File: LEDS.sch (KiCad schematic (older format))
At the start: 76 parts, among them Q1 MOSFET_N, Q2 MOSFET_N, Q3 MOSFET_N, Q4 MOSFET_N

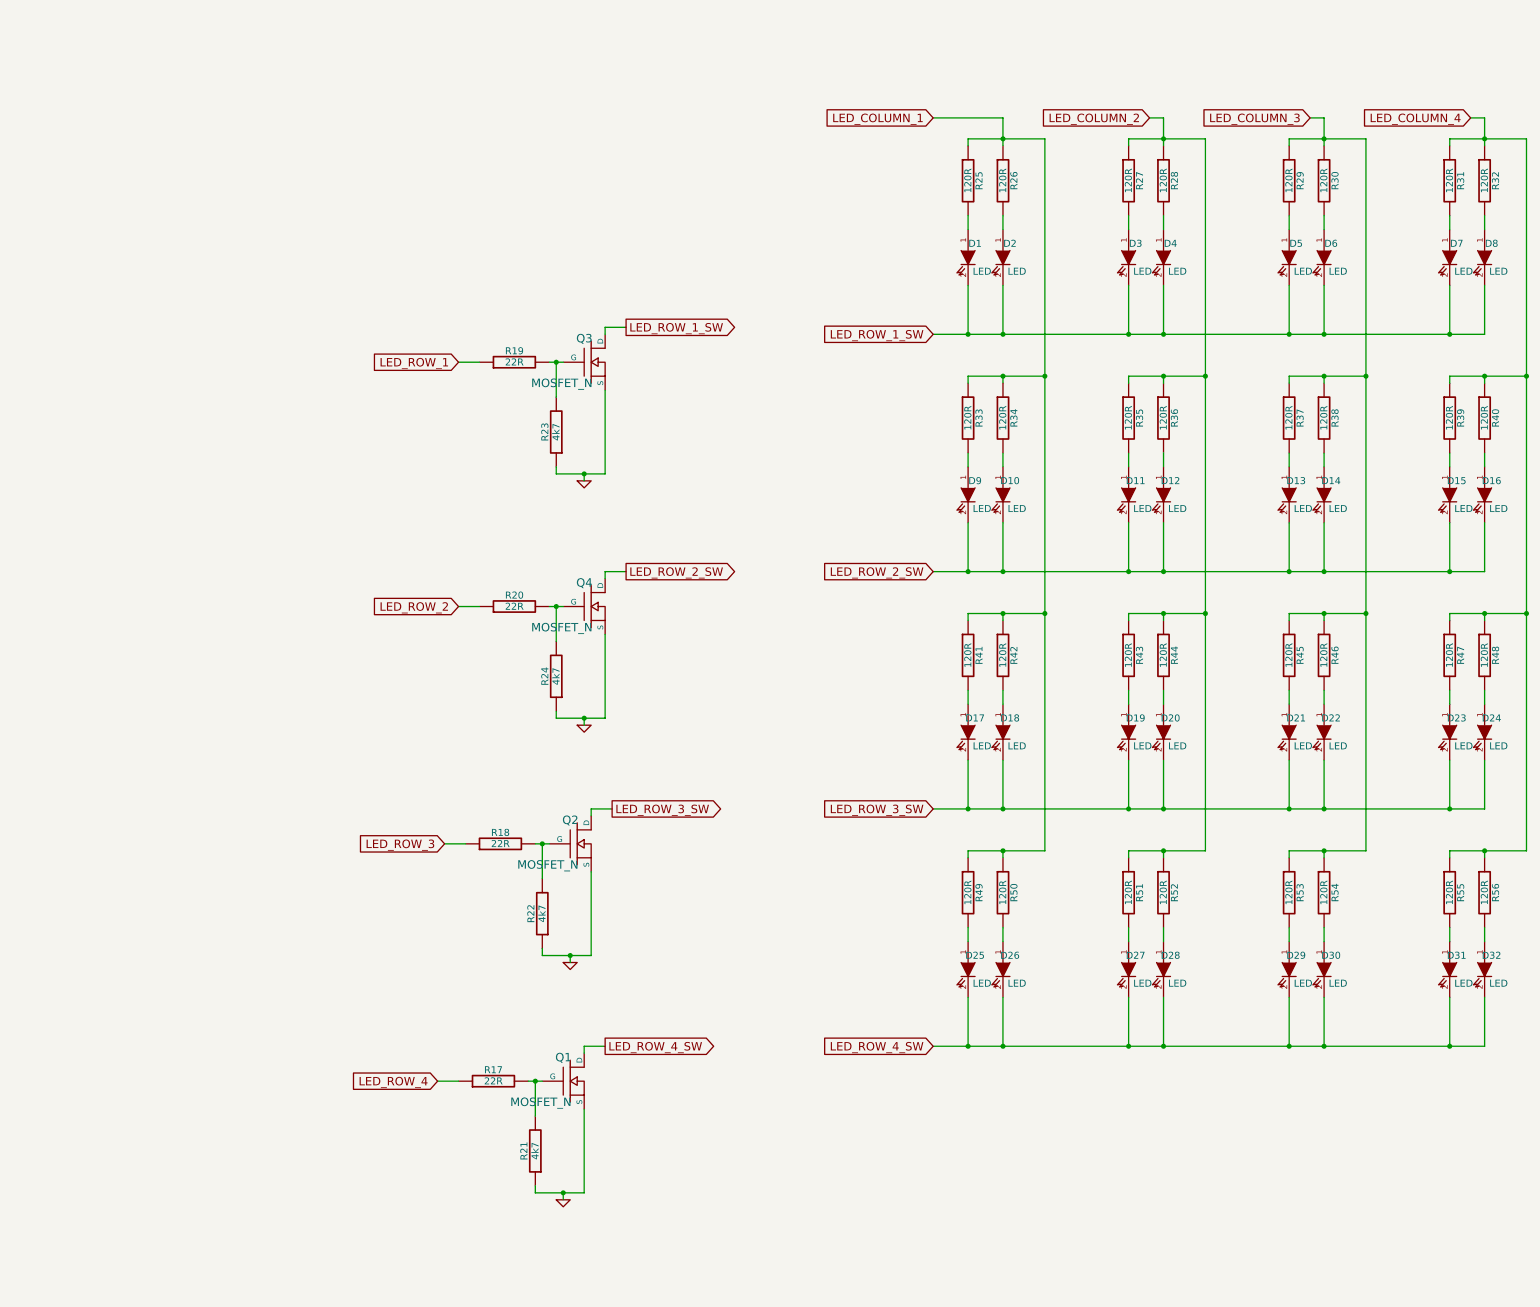
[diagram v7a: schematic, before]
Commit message: laying out 4 types of LED+electrode combos
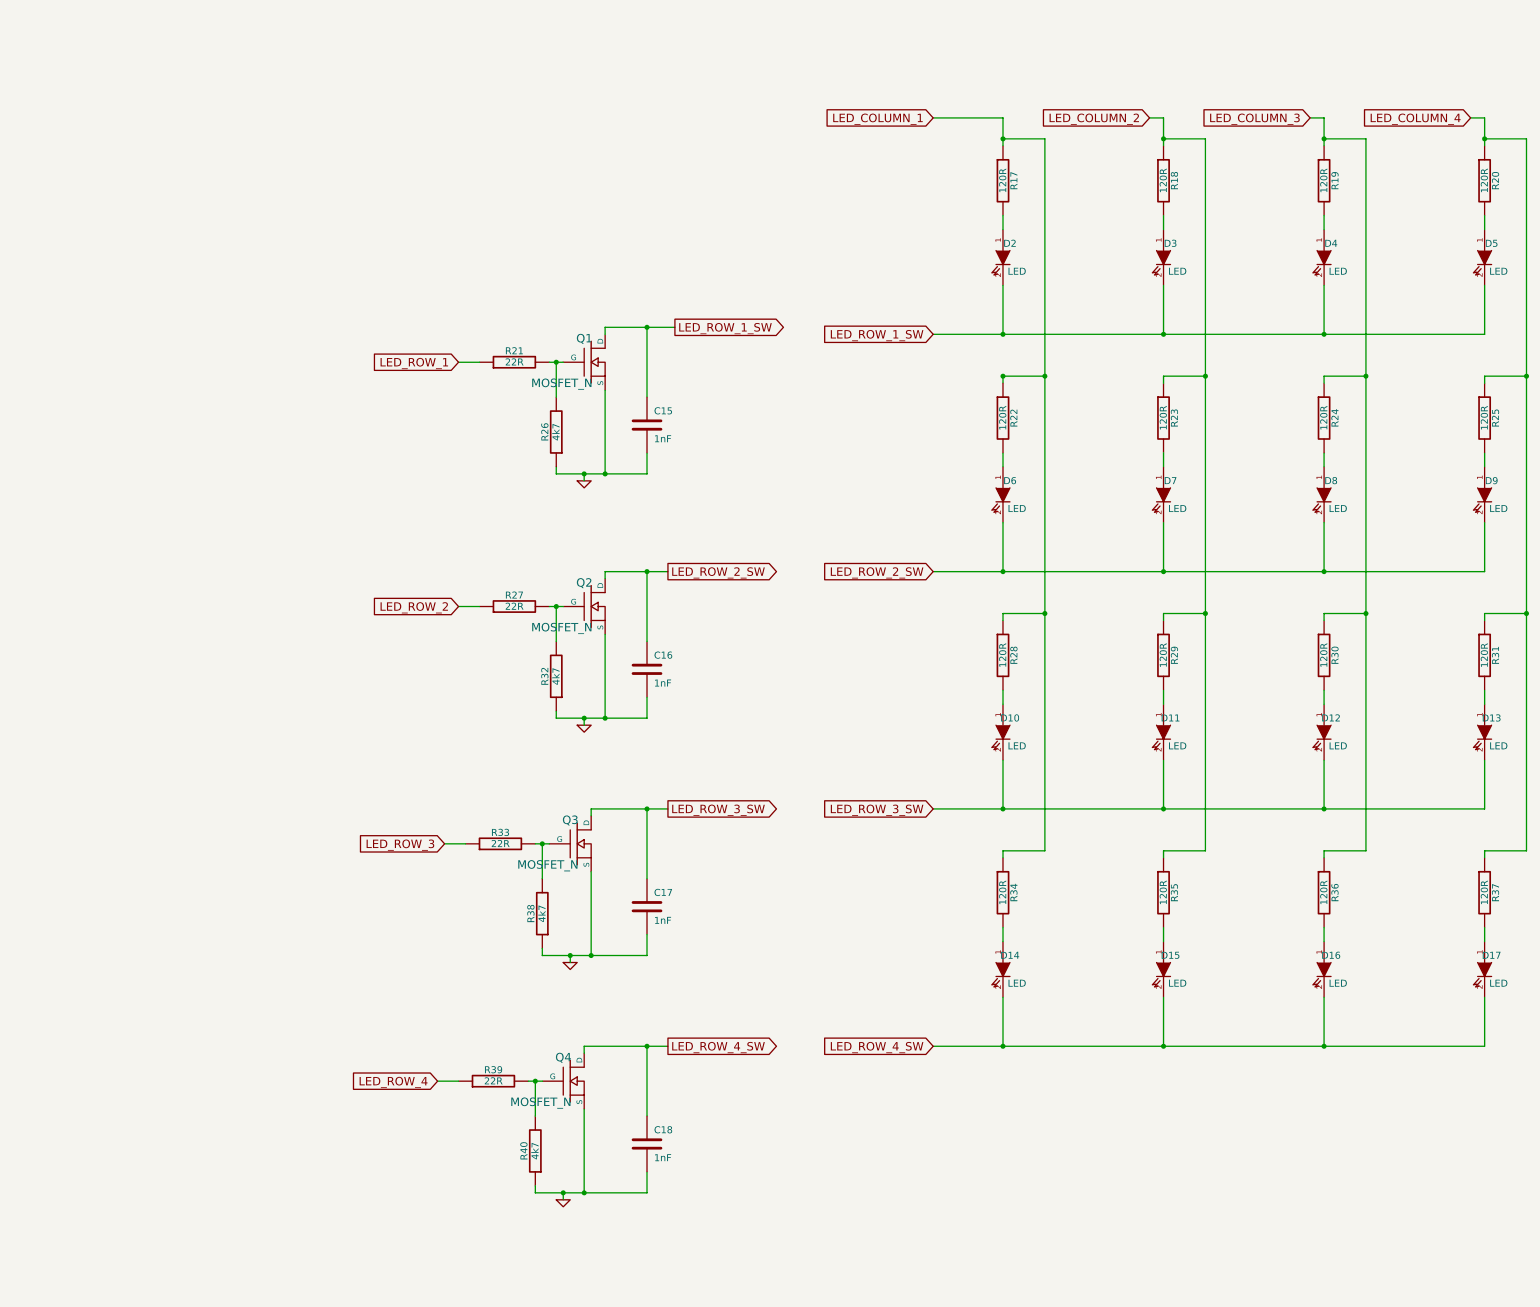
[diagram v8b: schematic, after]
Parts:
- removed D1, D11, D13, D15, D17, D19, D21, D23, D25, D27, D29, D3, D31, D5, D7, D9: LED, KPJA-2107SURCK, symbol LED
- removed R25, R27, R29, R31, R33, R35, R37, R39, R41, R43, R45, R47, R49, R51, R53, R55: 120R, SM0805, symbol R
- added C15, C16, C17, C18: 1nF, SM0805, symbol C
- D10: renamed from D18; footprint KPJA-2107SURCK -> SM0402
- D11: renamed from D20; footprint KPJA-2107SURCK -> SM0402
- D12: renamed from D22; footprint KPJA-2107SURCK -> SM0402
- D13: renamed from D24; footprint KPJA-2107SURCK -> SM0402
- D14: renamed from D26; footprint KPJA-2107SURCK -> SM0402
- D15: renamed from D28; footprint KPJA-2107SURCK -> SM0402
- D16: renamed from D30; footprint KPJA-2107SURCK -> SM0402
- D17: renamed from D32; footprint KPJA-2107SURCK -> SM0402
- D2: footprint KPJA-2107SURCK -> SM0402
- D3: renamed from D4; footprint KPJA-2107SURCK -> SM0402
- D4: renamed from D6; footprint KPJA-2107SURCK -> SM0402
- D5: renamed from D8; footprint KPJA-2107SURCK -> SM0402
- D6: renamed from D10; footprint KPJA-2107SURCK -> SM0402
- D7: renamed from D12; footprint KPJA-2107SURCK -> SM0402
- D8: renamed from D14; footprint KPJA-2107SURCK -> SM0402
- D9: renamed from D16; footprint KPJA-2107SURCK -> SM0402
- renumbered Q3 to Q1, Q4 to Q2, Q2 to Q3, Q1 to Q4, R26 to R17, R28 to R18, R30 to R19, R32 to R20, R19 to R21, R34 to R22, R36 to R23, R38 to R24, R40 to R25, R23 to R26, R20 to R27, R42 to R28, R44 to R29, R46 to R30, R48 to R31, R24 to R32, R18 to R33, R50 to R34, R52 to R35, R54 to R36, R56 to R37, R22 to R38, R17 to R39, R21 to R40
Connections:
- net GND: now also C15.2, C16.2, C17.2, C18.2
- net LED_ROW_1_SW: now also C15.1
- net LED_ROW_2_SW: now also C16.1
- net LED_ROW_3_SW: now also C17.1
- net LED_ROW_4_SW: now also C18.1
